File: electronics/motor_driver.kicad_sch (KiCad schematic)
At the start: 23 parts, among them J6 Conn_02x06_Counter_Clockwise, J7 MOT_CON, U7 BTT TMC5160 Pro

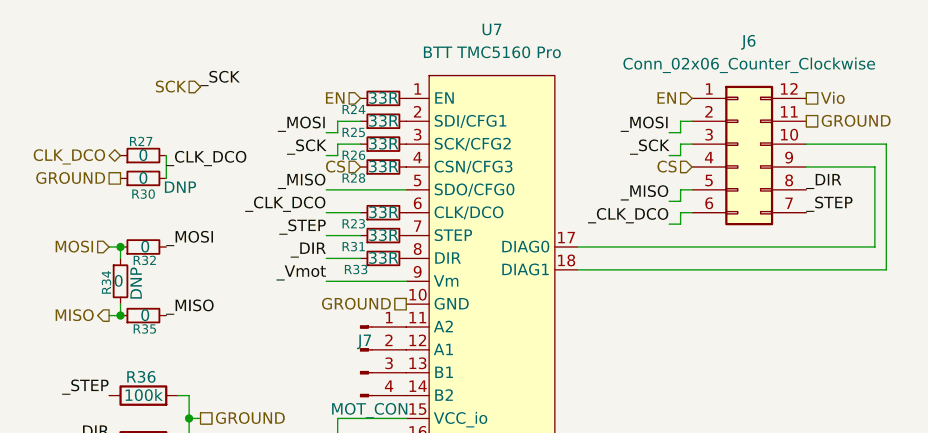
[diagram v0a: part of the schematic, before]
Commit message: Switching to a bigger PCB since cost seems negligible
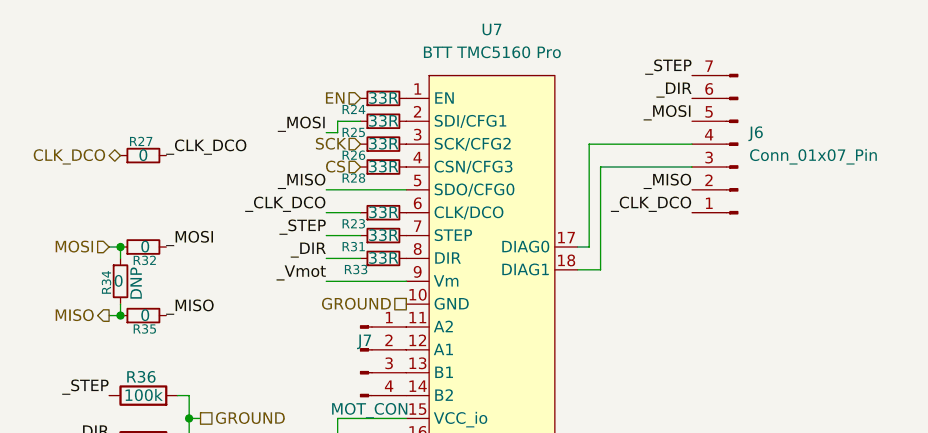
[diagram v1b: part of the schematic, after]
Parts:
- removed J6: Conn_02x06_Counter_Clockwise, Connector_PinSocket_2.54mm:PinSocket_2x06_P2.54mm_Vertical, symbol Connector_Generic:Conn_02x06_Counter_Clockwise
- removed R30: 0, Jumper:SolderJumper-2_P1.3mm_Open_Pad1.0x1.5mm, symbol Device:R_Small
- added J6: Conn_01x07_Pin, Connector_PinSocket_2.54mm:PinSocket_1x07_P2.54mm_Vertical, symbol Connector:Conn_01x07_Pin
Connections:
- net _CLK_DCO: now also J6.1 (Pin_1)
- net _DIR: now also J6.6 (Pin_6)
- net _MISO: now also J6.2 (Pin_2)
- net _MOSI: now also J6.5 (Pin_5)
- net _STEP: now also J6.7 (Pin_7)
- net at U7.18 (DIAG1): now also J6.3 (Pin_3)
- net at U7.17 (DIAG0): now also J6.4 (Pin_4)

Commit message: Updating electronics CAD post-production
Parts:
- removed R32, R34, R35: 0, Jumper:SolderJumper-2_P1.3mm_Open_Pad1.0x1.5mm, symbol Device:R_Small
- added R56: 0, Jumper:SolderJumper-2_P1.3mm_Open_Pad1.0x1.5mm, symbol Device:R
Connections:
- net GROUND: now also R36.1, R37.1; no longer R36.2, R37.2
- net MISO: now also J6.4 (Pin_4), U7.5 (SDO/CFG0), R56.2
- net MOSI: now also J6.3 (Pin_3), R25.1, R56.1
- net _CLK_DCO: now also J6.5 (Pin_5); no longer J6.1 (Pin_1)
- net _DIR: now also J6.7 (Pin_7); no longer J6.6 (Pin_6), R37.1
- net _STEP: now also J6.6 (Pin_6); no longer J6.7 (Pin_7), R36.1
- net at R33.2, U7.8 (DIR): now also R37.2
- net at U7.18 (DIAG1): now also J6.1 (Pin_1); no longer J6.3 (Pin_3)
- net at U7.17 (DIAG0): now also J6.2 (Pin_2); no longer J6.4 (Pin_4)
- net at R31.2, U7.7 (STEP): now also R36.2
- removed net _MISO: J6.2 (Pin_2), U7.5 (SDO/CFG0)
- removed net _MOSI: J6.5 (Pin_5), R25.1
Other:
- moved on the sheet: R27, R31, R33, R36, R37

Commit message: Some vibe coding to set up project structure. Almost all of the code will be rewritten to my standards
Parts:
- C13, C14, J7, L1, R23, R24, R25, R26, R27, R28, R31, R33, R36, R37, R56, U7: msrcrt (none) -> NA
- C15, C16: msrcrt (none) -> Y
- F4, J6: msrcrt (none) -> N
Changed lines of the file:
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@@
+			)
+		)
+		(property "msrcrt" "NA"
+			(at 62.23 45.72 90)
+			(effects
+				(font
+					(size 1.27 1.27)
+				)
+				(hide yes)
 			)
 		)
@@
 			)
 		)
+		(property "msrcrt" "NA"
+			(at 62.23 43.18 90)
+			(effects
+				(font
+					(size 1.27 1.27)
+				)
+				(hide yes)
+			)
+		)
 		(pin "1"
 		)
@@
 			)
 		)
+		(property "msrcrt" "NA"
+			(at 31.75 30.48 90)
+			(effects
+				(font
+					(size 1.27 1.27)
+				)
+				(hide yes)
+			)
+		)
 		(pin "1"
 		)
@@
 			)
 		)
+		(property "msrcrt" "NA"
+			(at 34.29 50.8 0)
+			(effects
+				(font
+					(size 1.27 1.27)
+				)
+				(hide yes)
+			)
+		)
 		(pin "1"
 		)
@@
 			)
 		)
+		(property "msrcrt" "Y"
+			(at 62.23 119.38 90)
+			(effects
+				(font
+					(size 1.27 1.27)
+				)
+				(hide yes)
+			)
+		)
 		(pin "2"
 		)
@@
 			)
 		)
+		(property "msrcrt" "NA"
+			(at 62.23 48.26 90)
+			(effects
+				(font
+					(size 1.27 1.27)
+				)
+				(hide yes)
+			)
+		)
 		(pin "1"
 		)
@@
 			)
 		)
+		(property "msrcrt" "NA"
+			(at 49.53 109.22 90)
+			(effects
+				(font
+					(size 1.27 1.27)
+				)
+				(hide yes)
+			)
+		)
 		(pin "2"
 		)
@@
 			)
 		)
+		(property "msrcrt" "NA"
+			(at 38.1 60.96 90)
+			(effects
+				(font
+					(size 1.27 1.27)
+				)
+				(hide yes)
+			)
+		)
 		(pin "1"
 		)
@@
 			)
 		)
+		(property "msrcrt" "NA"
+			(at 59.69 71.12 0)
+			(effects
+				(font
+					(size 1.27 1.27)
+				)
+				(hide yes)
+			)
+		)
 		(pin "1"
 		)
@@
 			)
 		)
+		(property "msrcrt" "NA"
+			(at 46.99 67.31 90)
+			(effects
+				(font
+					(size 1.27 1.27)
+				)
+				(hide yes)
+			)
+		)
 		(pin "2"
 		)
@@
 			)
 		)
+		(property "msrcrt" "NA"
+			(at 41.91 67.31 90)
+			(effects
+				(font
+					(size 1.27 1.27)
+				)
+				(hide yes)
+			)
+		)
 		(pin "2"
 		)
@@
 		)
 		(property "DNP" ""
+			(at 60.96 83.82 90)
+			(effects
+				(font
+					(size 1.27 1.27)
+				)
+				(hide yes)
+			)
+		)
+		(property "msrcrt" "NA"
 			(at 60.96 83.82 90)
 			(effects
@@
 			)
 		)
+		(property "msrcrt" "NA"
+			(at 62.23 50.8 90)
+			(effects
+				(font
+					(size 1.27 1.27)
+				)
+				(hide yes)
+			)
+		)
 		(pin "1"
 		)
@@
 			)
 		)
+		(property "msrcrt" "N"
+			(at 101.6 48.26 0)
+			(effects
+				(font
+					(size 1.27 1.27)
+				)
+				(hide yes)
+			)
+		)
 		(pin "7"
 		)
@@
 			)
 		)
+		(property "msrcrt" "NA"
+			(at 67.31 40.64 0)
+			(effects
+				(font
+					(size 1.27 1.27)
+				)
+				(hide yes)
+			)
+		)
 		(pin "2"
 		)
@@
 			)
 		)
+		(property "msrcrt" "Y"
+			(at 62.23 124.46 90)
+			(effects
+				(font
+					(size 1.27 1.27)
+				)
+				(hide yes)
+			)
+		)
 		(pin "2"
 		)
@@
 			)
 		)
+		(property "msrcrt" "NA"
+			(at 62.23 105.41 90)
+			(effects
+				(font
+					(size 1.27 1.27)
+				)
+				(hide yes)
+			)
+		)
 		(pin "2"
 		)
@@
 			)
 		)
+		(property "msrcrt" "NA"
+			(at 62.23 55.88 90)
+			(effects
+				(font
+					(size 1.27 1.27)
+				)
+				(hide yes)
+			)
+		)
 		(pin "1"
 		)
@@
 			)
 		)
+		(property "msrcrt" "N"
+			(at 50.8 113.03 90)
+			(effects
+				(font
+					(size 1.27 1.27)
+				)
+				(hide yes)
+			)
+		)
 		(pin "1"
 		)
@@
 			(at 38.1 58.42 90)
 			(effects
+				(font
+					(size 1.27 1.27)
+				)
+				(hide yes)
+			)
+		)
+		(property "msrcrt" "NA"
+			(at 38.1 58.42 90)
+			(effects
